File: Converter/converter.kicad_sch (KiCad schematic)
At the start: 32 parts, among them IC1 NCP5109ADR2G, IC2 NCP5109ADR2G, J1 XT30, J2 XT30

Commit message: laid out PCB rev C
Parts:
- renumbered C_{smooth}6 to C_{smooth}4, C_{smooth}7 to C_{smooth}5, J2 to J3, J1 to J4, L1 to L2
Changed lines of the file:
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@@
 		(dnp no)
 		(fields_autoplaced yes)
-		(property "Reference" "J2"
+		(property "Reference" "J3"
 			(at 125.095 62.2299 0)
 			(effects
@@
 			(project ""
 				(path "/98ee8313-37ab-4329-91ab-b5710476f82f/66de8ce3-68f9-4d35-858c-1420192a373c"
-					(reference "J2")
+					(reference "J3")
 					(unit 1)
 				)
@@
 		(dnp no)
 		(fields_autoplaced yes)
-		(property "Reference" "#PWR022"
+		(property "Reference" "#PWR025"
 			(at 74.93 144.78 0)
 			(effects
@@
 			(project "Supercap"
 				(path "/98ee8313-37ab-4329-91ab-b5710476f82f/66de8ce3-68f9-4d35-858c-1420192a373c"
-					(reference "#PWR022")
+					(reference "#PWR025")
 					(unit 1)
 				)
@@
 		(dnp no)
 		(fields_autoplaced yes)
-		(property "Reference" "C_{smooth}7"
+		(property "Reference" "C_{smooth}5"
 			(at 78.74 133.3499 0)
 			(effects
@@
 			(project "Supercap"
 				(path "/98ee8313-37ab-4329-91ab-b5710476f82f/66de8ce3-68f9-4d35-858c-1420192a373c"
-					(reference "C_{smooth}7")
+					(reference "C_{smooth}5")
 					(unit 1)
 				)
@@
 		(on_board yes)
 		(dnp no)
-		(property "Reference" "J1"
+		(property "Reference" "J4"
 			(at 138.176 64.516 0)
 			(effects
@@
 			(project ""
 				(path "/98ee8313-37ab-4329-91ab-b5710476f82f/66de8ce3-68f9-4d35-858c-1420192a373c"
-					(reference "J1")
+					(reference "J4")
 					(unit 1)
 				)
@@
 		(dnp no)
 		(fields_autoplaced yes)
-		(property "Reference" "#PWR027"
+		(property "Reference" "#PWR030"
 			(at 182.245 151.765 0)
 			(effects
@@
 			(project "Supercap"
 				(path "/98ee8313-37ab-4329-91ab-b5710476f82f/66de8ce3-68f9-4d35-858c-1420192a373c"
-					(reference "#PWR027")
+					(reference "#PWR030")
 					(unit 1)
 				)
@@
 		(dnp no)
 		(fields_autoplaced yes)
-		(property "Reference" "#PWR029"
+		(property "Reference" "#PWR031"
 			(at 219.075 62.23 0)
 			(effects
@@
 			(project "Supercap"
 				(path "/98ee8313-37ab-4329-91ab-b5710476f82f/66de8ce3-68f9-4d35-858c-1420192a373c"
-					(reference "#PWR029")
+					(reference "#PWR031")
 					(unit 1)
 				)
@@
 		(dnp no)
 		(fields_autoplaced yes)
-		(property "Reference" "#PWR028"
+		(property "Reference" "#PWR029"
 			(at 182.245 81.28 0)
 			(effects
@@
 			(project "Supercap"
 				(path "/98ee8313-37ab-4329-91ab-b5710476f82f/66de8ce3-68f9-4d35-858c-1420192a373c"
-					(reference "#PWR028")
+					(reference "#PWR029")
 					(unit 1)
 				)
@@
 		(dnp no)
 		(fields_autoplaced yes)
-		(property "Reference" "L1"
+		(property "Reference" "L2"
 			(at 132.08 54.61 90)
 			(effects
@@
 			(project "Supercap"
 				(path "/98ee8313-37ab-4329-91ab-b5710476f82f/66de8ce3-68f9-4d35-858c-1420192a373c"
-					(reference "L1")
+					(reference "L2")
 					(unit 1)
 				)
@@
 		(dnp no)
 		(fields_autoplaced yes)
-		(property "Reference" "#PWR025"
+		(property "Reference" "#PWR027"
 			(at 85.09 154.94 0)
 			(effects
@@
 			(project "Supercap"
 				(path "/98ee8313-37ab-4329-91ab-b5710476f82f/66de8ce3-68f9-4d35-858c-1420192a373c"
-					(reference "#PWR025")
+					(reference "#PWR027")
 					(unit 1)
 				)
@@
 		(dnp no)
 		(fields_autoplaced yes)
-		(property "Reference" "C_{smooth}6"
+		(property "Reference" "C_{smooth}4"
 			(at 78.74 104.1399 0)
 			(effects
@@
 			(project "Supercap"
 				(path "/98ee8313-37ab-4329-91ab-b5710476f82f/66de8ce3-68f9-4d35-858c-1420192a373c"
-					(reference "C_{smooth}6")
+					(reference "C_{smooth}4")
 					(unit 1)
 				)
@@
 		(dnp no)
 		(fields_autoplaced yes)
-		(property "Reference" "#PWR026"
+		(property "Reference" "#PWR028"
 			(at 103.505 81.28 0)
 			(effects
@@
 			(project ""
 				(path "/98ee8313-37ab-4329-91ab-b5710476f82f/66de8ce3-68f9-4d35-858c-1420192a373c"
-					(reference "#PWR026")
+					(reference "#PWR028")
 					(unit 1)
 				)
@@
 		(dnp no)
 		(fields_autoplaced yes)
-		(property "Reference" "#PWR024"
+		(property "Reference" "#PWR026"
 			(at 85.09 125.73 0)
 			(effects
@@
 			(project "Supercap"
 				(path "/98ee8313-37ab-4329-91ab-b5710476f82f/66de8ce3-68f9-4d35-858c-1420192a373c"
-					(reference "#PWR024")
+					(reference "#PWR026")
 					(unit 1)
 				)
@@
 		(dnp no)
 		(fields_autoplaced yes)
-		(property "Reference" "#PWR021"
+		(property "Reference" "#PWR024"
 			(at 74.93 115.57 0)
 			(effects
@@
 			(project "Supercap"
 				(path "/98ee8313-37ab-4329-91ab-b5710476f82f/66de8ce3-68f9-4d35-858c-1420192a373c"
-					(reference "#PWR021")
+					(reference "#PWR024")
 					(unit 1)
 				)

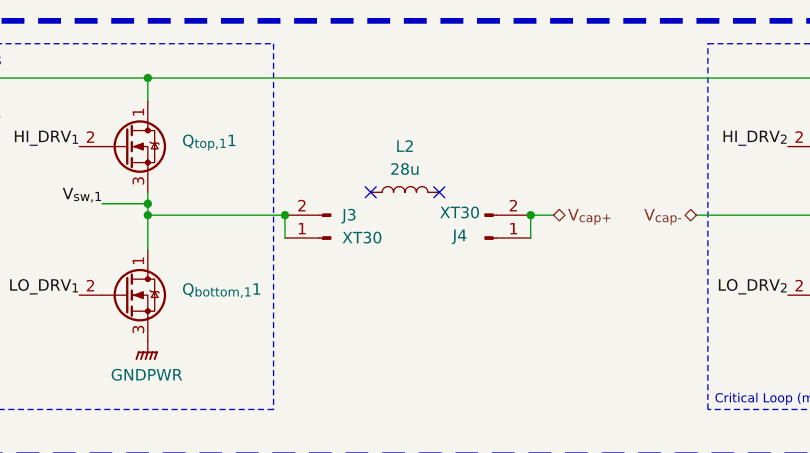
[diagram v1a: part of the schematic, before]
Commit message: added parallel capacitance, minor cleanup to design - jed review + approval
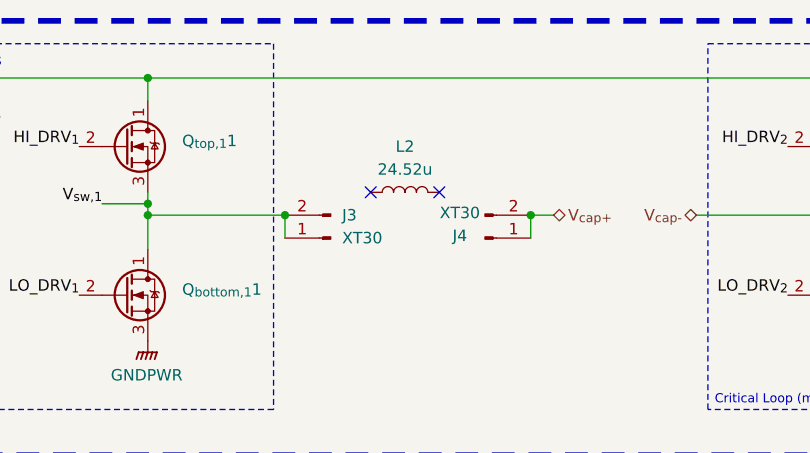
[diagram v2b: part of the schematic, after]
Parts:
- J3, J4: now left out of the parts list
- L2: value 28u -> 24.52u

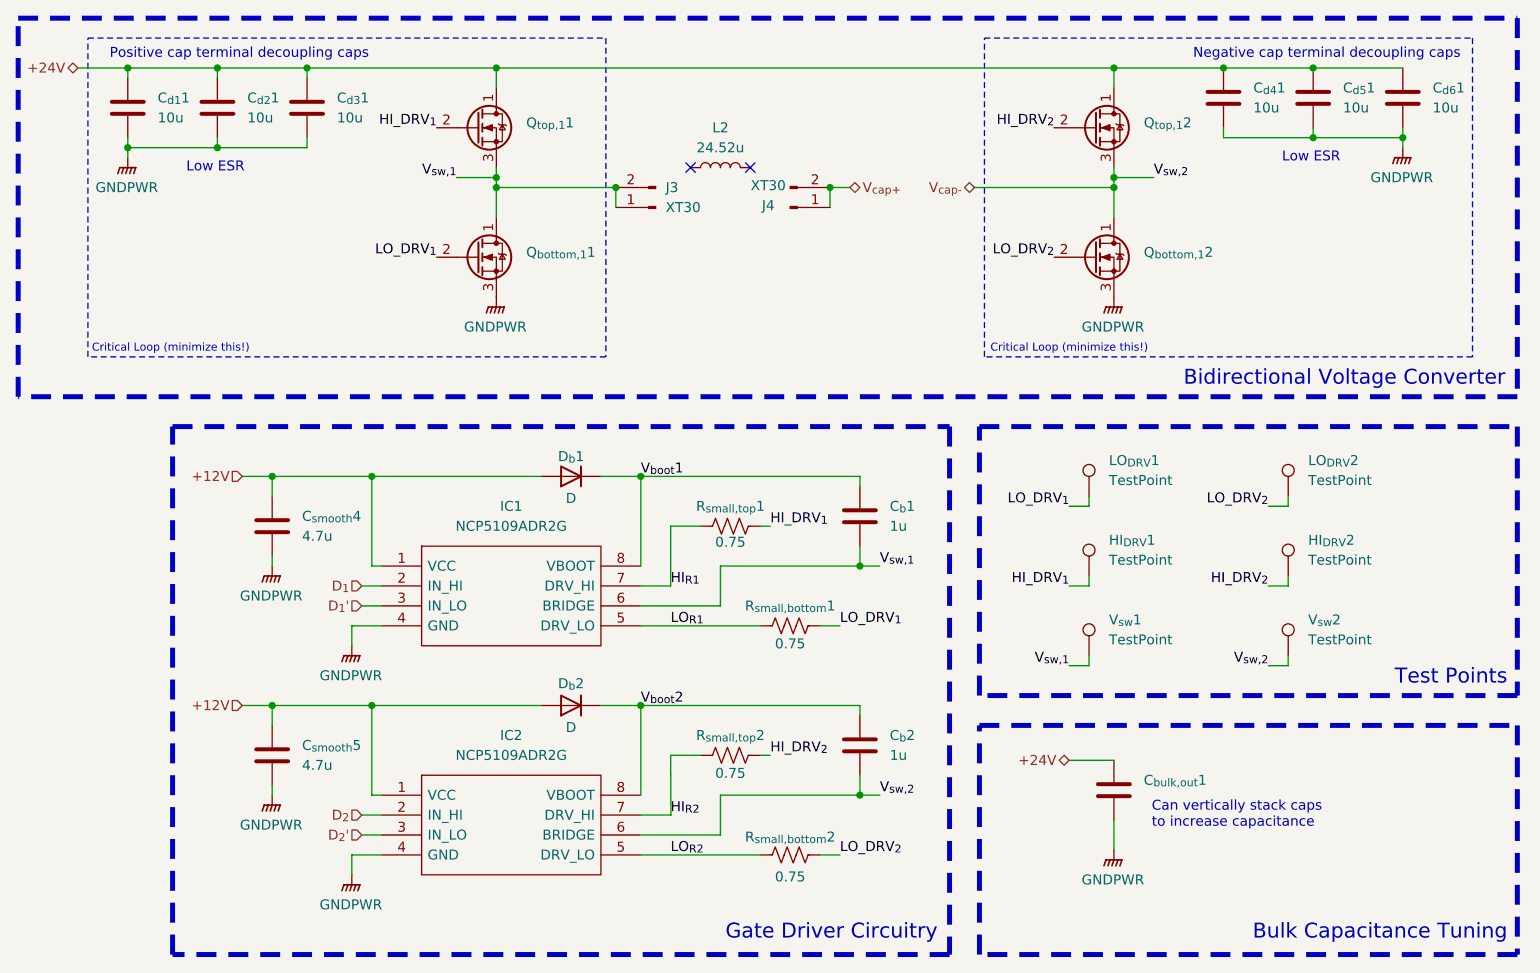
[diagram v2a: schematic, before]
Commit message: added heatsinks + more bulk capacitance footprints
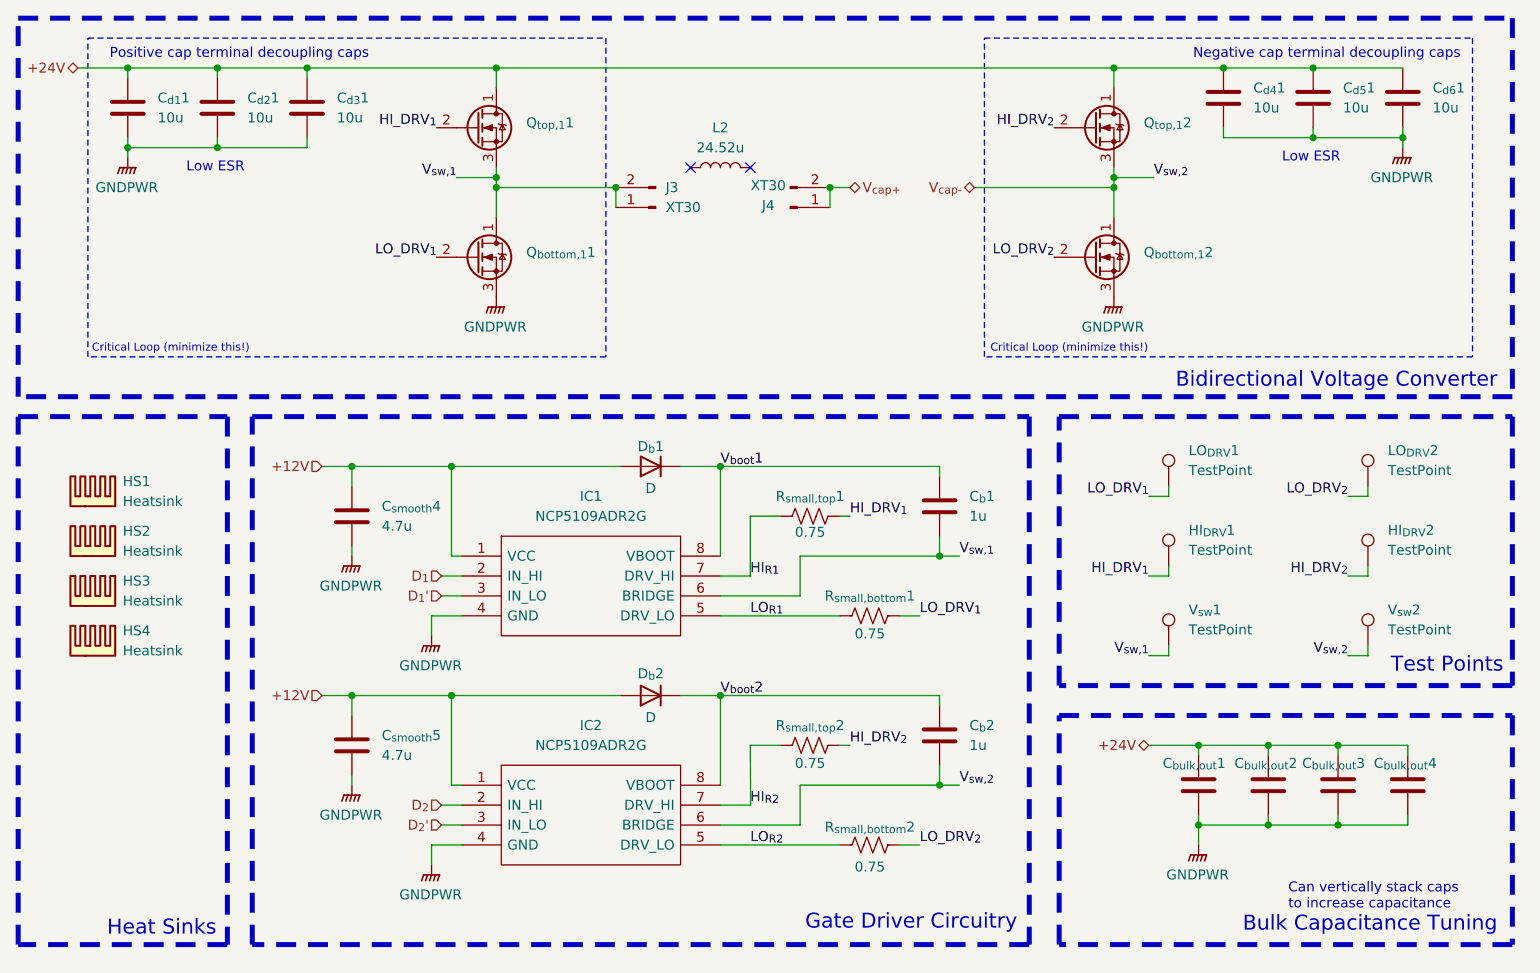
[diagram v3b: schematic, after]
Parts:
- added C_{bulk,out}2, C_{bulk,out}3, C_{bulk,out}4: ~, Capacitor_SMD:C_0603_1608Metric_Pad1.08x0.95mm_HandSolder, symbol Device:C
- added HS1, HS2, HS3, HS4: Heatsink, symbol Mechanical:Heatsink
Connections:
- net +24V: now also C_{bulk,out}2.1, C_{bulk,out}3.1, C_{bulk,out}4.1
- net GNDPWR: now also C_{bulk,out}2.2, C_{bulk,out}3.2, C_{bulk,out}4.2
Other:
- note added: "Heat Sinks"
- moved on the sheet: C_{bulk,out}1, C_{b}1, C_{b}2, C_{smooth}4, C_{smooth}5, D_{b}1, D_{b}2, HI_{DRV}1, HI_{DRV}2, IC1, IC2, LO_{DRV}1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

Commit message: added better smoothing behavior to power supplies and op-amps as per application notes, switched resistors to op-amp with higher values
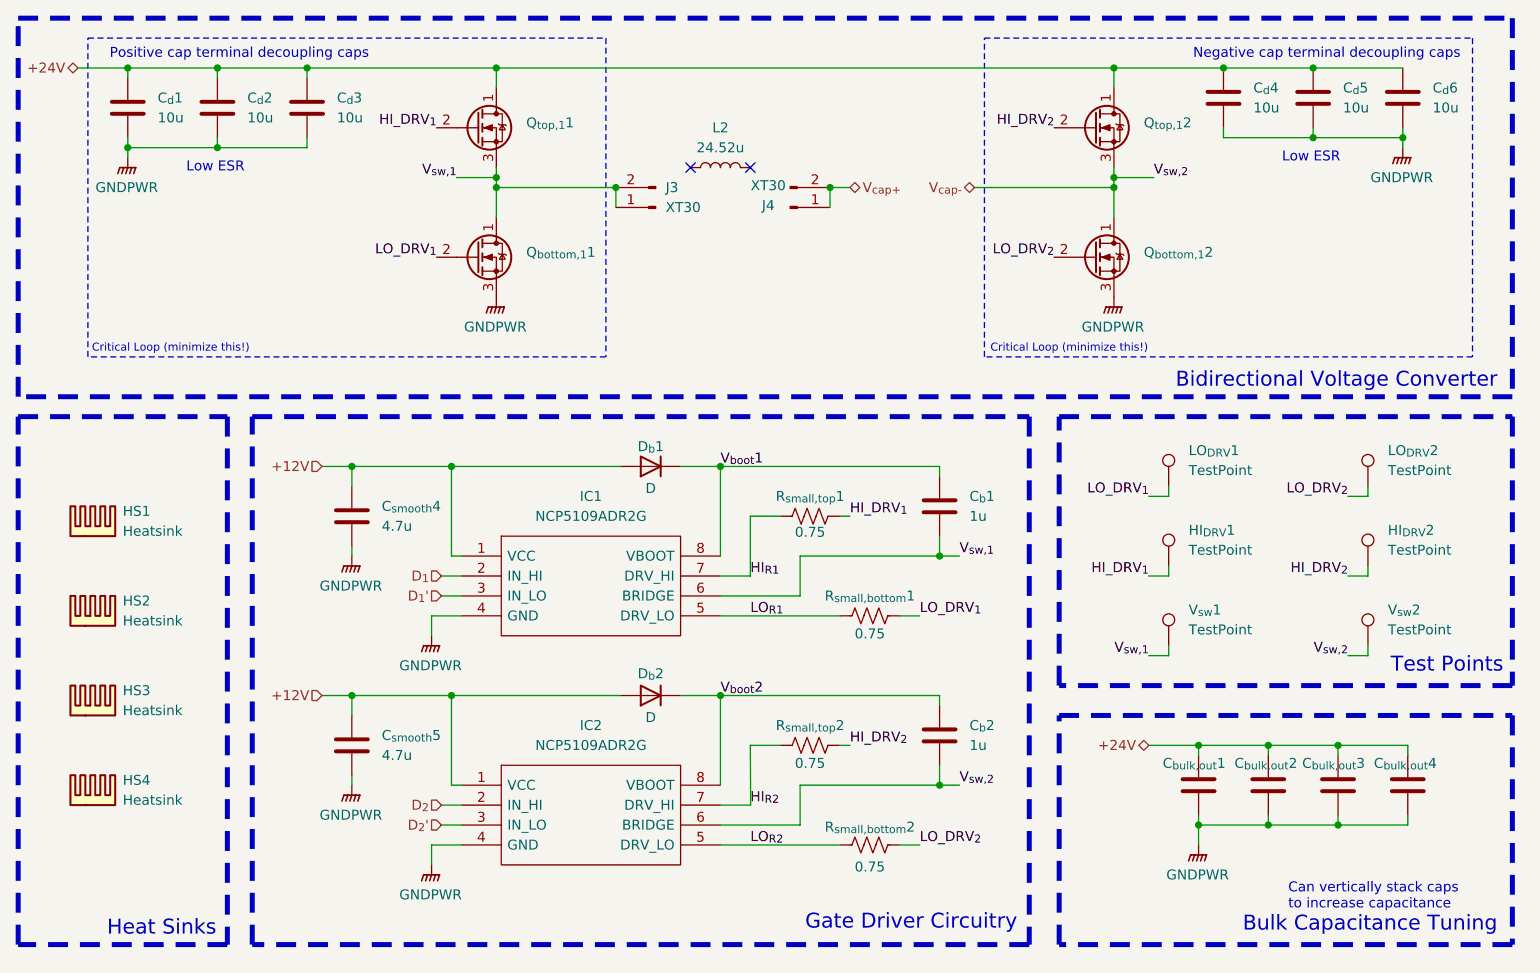
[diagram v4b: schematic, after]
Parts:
- renumbered C_{d1}1 to C_{d}1, C_{d2}1 to C_{d}2, C_{d3}1 to C_{d}3, C_{d4}1 to C_{d}4, C_{d5}1 to C_{d}5, C_{d6}1 to C_{d}6
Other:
- moved on the sheet: HS1, HS2, HS3, HS4
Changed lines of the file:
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@@
 	(symbol
 		(lib_id "Mechanical:Heatsink")
-		(at 52.07 115.57 0)
+		(at 52.07 129.54 0)
 		(unit 1)
 		(exclude_from_sim no)
@@
 		(fields_autoplaced yes)
 		(property "Reference" "HS3"
-			(at 55.88 112.3949 0)
+			(at 55.88 126.3649 0)
 			(effects
 				(font
@@
 		)
 		(property "Value" "Heatsink"
-			(at 55.88 114.9349 0)
+			(at 55.88 128.9049 0)
 			(effects
 				(font
@@
 		)
 		(property "Footprint" ""
-			(at 52.3748 115.57 0)
+			(at 52.3748 129.54 0)
 			(effects
 				(font
@@
 		)
 		(property "Datasheet" "https://www.mouser.com/datasheet/3/6118/1/hsb01_080808.pdf"
-			(at 52.3748 115.57 0)
+			(at 52.3748 129.54 0)
 			(effects
 				(font
@@
 		)
 		(property "Description" "Heatsink"
-			(at 52.07 115.57 0)
+			(at 52.07 129.54 0)
 			(effects
 				(font
@@
 		)
 		(property "Manufacturer_Part_Number" "HSB01-080808 "
-			(at 52.07 115.57 0)
+			(at 52.07 129.54 0)
 			(effects
 				(font
@@
 		)
 		(property "Mouser Part Number" "490-HSB01-080808 "
-			(at 52.07 115.57 0)
+			(at 52.07 129.54 0)
 			(effects
 				(font
@@
 		(on_board yes)
 		(dnp no)
-		(property "Reference" "C_{d3}1"
+		(property "Reference" "C_{d}3"
 			(at 83.185 50.7999 0)
 			(effects
@@
 			(project "Supercap"
 				(path "/98ee8313-37ab-4329-91ab-b5710476f82f/66de8ce3-68f9-4d35-858c-1420192a373c"
-					(reference "C_{d3}1")
+					(reference "C_{d}3")
 					(unit 1)
 				)
@@
 	(symbol
 		(lib_id "Mechanical:Heatsink")
-		(at 52.07 121.92 0)
+		(at 52.07 140.97 0)
 		(unit 1)
 		(exclude_from_sim no)
@@
 		(fields_autoplaced yes)
 		(property "Reference" "HS4"
-			(at 55.88 118.7449 0)
+			(at 55.88 137.7949 0)
 			(effects
 				(font
@@
 		)
 		(property "Value" "Heatsink"
-			(at 55.88 121.2849 0)
+			(at 55.88 140.3349 0)
 			(effects
 				(font
@@
 		)
 		(property "Footprint" ""
-			(at 52.3748 121.92 0)
+			(at 52.3748 140.97 0)
 			(effects
 				(font
@@
 		)
 		(property "Datasheet" "https://www.mouser.com/datasheet/3/6118/1/hsb01_080808.pdf"
-			(at 52.3748 121.92 0)
+			(at 52.3748 140.97 0)
 			(effects
 				(font
@@
 		)
 		(property "Description" "Heatsink"
-			(at 52.07 121.92 0)
+			(at 52.07 140.97 0)
 			(effects
 				(font
@@
 		)
 		(property "Manufacturer_Part_Number" "HSB01-080808 "
-			(at 52.07 121.92 0)
+			(at 52.07 140.97 0)
 			(effects
 				(font
@@
 		)
 		(property "Mouser Part Number" "490-HSB01-080808 "
-			(at 52.07 121.92 0)
+			(at 52.07 140.97 0)
 			(effects
 				(font
@@
 	(symbol
 		(lib_id "Mechanical:Heatsink")
-		(at 52.07 109.22 0)
+		(at 52.07 118.11 0)
 		(unit 1)
 		(exclude_from_sim no)
@@
 		(fields_autoplaced yes)
 		(property "Reference" "HS2"
-			(at 55.88 106.0449 0)
+			(at 55.88 114.9349 0)
 			(effects
 				(font
@@
 		)
 		(property "Value" "Heatsink"
-			(at 55.88 108.5849 0)
+			(at 55.88 117.4749 0)
 			(effects
 				(font
@@
 		)
 		(property "Footprint" ""
-			(at 52.3748 109.22 0)
+			(at 52.3748 118.11 0)
 			(effects
 				(font
@@
 		)
 		(property "Datasheet" "https://www.mouser.com/datasheet/3/6118/1/hsb01_080808.pdf"
-			(at 52.3748 109.22 0)
+			(at 52.3748 118.11 0)
 			(effects
 				(font
@@
 		)
 		(property "Description" "Heatsink"
-			(at 52.07 109.22 0)
+			(at 52.07 118.11 0)
 			(effects
 				(font
@@
 		)
 		(property "Manufacturer_Part_Number" "HSB01-080808 "
-			(at 52.07 109.22 0)
+			(at 52.07 118.11 0)
 			(effects
 				(font
@@
 		)
 		(property "Mouser Part Number" "490-HSB01-080808 "
-			(at 52.07 109.22 0)
+			(at 52.07 118.11 0)
 			(effects
 				(font
@@
 		(on_board yes)
 		(dnp no)
-		(property "Reference" "C_{d4}1"
+		(property "Reference" "C_{d}4"
 			(at 200.025 49.5299 0)
 			(effects
@@
 			(project "Supercap"
 				(path "/98ee8313-37ab-4329-91ab-b5710476f82f/66de8ce3-68f9-4d35-858c-1420192a373c"
-					(reference "C_{d4}1")
+					(reference "C_{d}4")
 					(unit 1)
 				)
@@
 		(on_board yes)
 		(dnp no)
-		(property "Reference" "C_{d1}1"
+		(property "Reference" "C_{d}1"
 			(at 60.325 50.7999 0)
 			(effects
@@
 			(project "Supercap"
 				(path "/98ee8313-37ab-4329-91ab-b5710476f82f/66de8ce3-68f9-4d35-858c-1420192a373c"
-					(reference "C_{d1}1")
+					(reference "C_{d}1")
 					(unit 1)
 				)
@@
 		(on_board yes)
 		(dnp no)
-		(property "Reference" "C_{d2}1"
+		(property "Reference" "C_{d}2"
 			(at 71.755 50.7999 0)
 			(effects
@@
 			(project "Supercap"
 				(path "/98ee8313-37ab-4329-91ab-b5710476f82f/66de8ce3-68f9-4d35-858c-1420192a373c"
-					(reference "C_{d2}1")
+					(reference "C_{d}2")
 					(unit 1)
 				)
@@
 	(symbol
 		(lib_id "Mechanical:Heatsink")
-		(at 52.07 102.87 0)
+		(at 52.07 106.68 0)
 		(unit 1)
 		(exclude_from_sim no)
@@
 		(fields_autoplaced yes)
 		(property "Reference" "HS1"
-			(at 55.88 99.6949 0)
+			(at 55.88 103.5049 0)
 			(effects
 				(font
@@
 		)
 		(property "Value" "Heatsink"
-			(at 55.88 102.2349 0)
+			(at 55.88 106.0449 0)
 			(effects
 				(font
@@
 		)
 		(property "Footprint" ""
-			(at 52.3748 102.87 0)
+			(at 52.3748 106.68 0)
 			(effects
 				(font
@@
 		)
 		(property "Datasheet" "https://www.mouser.com/datasheet/3/6118/1/hsb01_080808.pdf"
-			(at 52.3748 102.87 0)
+			(at 52.3748 106.68 0)
 			(effects
 				(font
@@
 		)
 		(property "Description" "Heatsink"
-			(at 52.07 102.87 0)
+			(at 52.07 106.68 0)
 			(effects
 				(font
@@
 		)
 		(property "Manufacturer_Part_Number" "HSB01-080808 "
-			(at 52.07 102.87 0)
+			(at 52.07 106.68 0)
 			(effects
 				(font
@@
 		)
 		(property "Mouser Part Number" "490-HSB01-080808 "
-			(at 52.07 102.87 0)
+			(at 52.07 106.68 0)
 			(effects
 				(font
@@
 		(on_board yes)
 		(dnp no)
-		(property "Reference" "C_{d6}1"
+		(property "Reference" "C_{d}6"
 			(at 222.885 49.5299 0)
 			(effects
@@
 			(project "Supercap"
 				(path "/98ee8313-37ab-4329-91ab-b5710476f82f/66de8ce3-68f9-4d35-858c-1420192a373c"
-					(reference "C_{d6}1")
+					(reference "C_{d}6")
 					(unit 1)
 				)
@@
 		(on_board yes)
 		(dnp no)
-		(property "Reference" "C_{d5}1"
+		(property "Reference" "C_{d}5"
 			(at 211.455 49.5299 0)
 			(effects
@@
 			(project "Supercap"
 				(path "/98ee8313-37ab-4329-91ab-b5710476f82f/66de8ce3-68f9-4d35-858c-1420192a373c"
-					(reference "C_{d5}1")
+					(reference "C_{d}5")
 					(unit 1)
 				)
